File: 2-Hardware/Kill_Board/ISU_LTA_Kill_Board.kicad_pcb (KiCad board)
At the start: 2 copper layers, 157.5 x 36.2 mm, 30 parts, among them P1 CONN_01X02, P10 CONN_2, P11 CONN_2, P12 CONN_2, P2 CONN_01X02, P3 CONN_01X02, P4 CONN_01X03, P5 CONN_01X03, P6 CONN_01X03, P7 CONN_2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

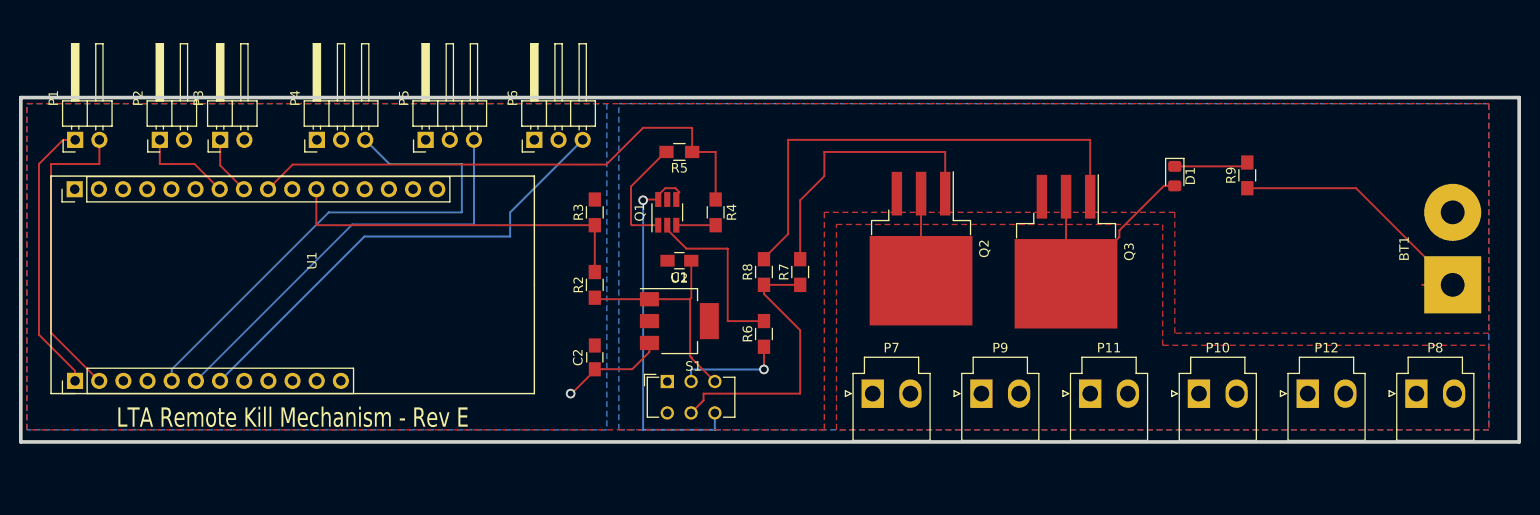
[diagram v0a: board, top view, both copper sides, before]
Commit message: Updated to have BEC and level shifter
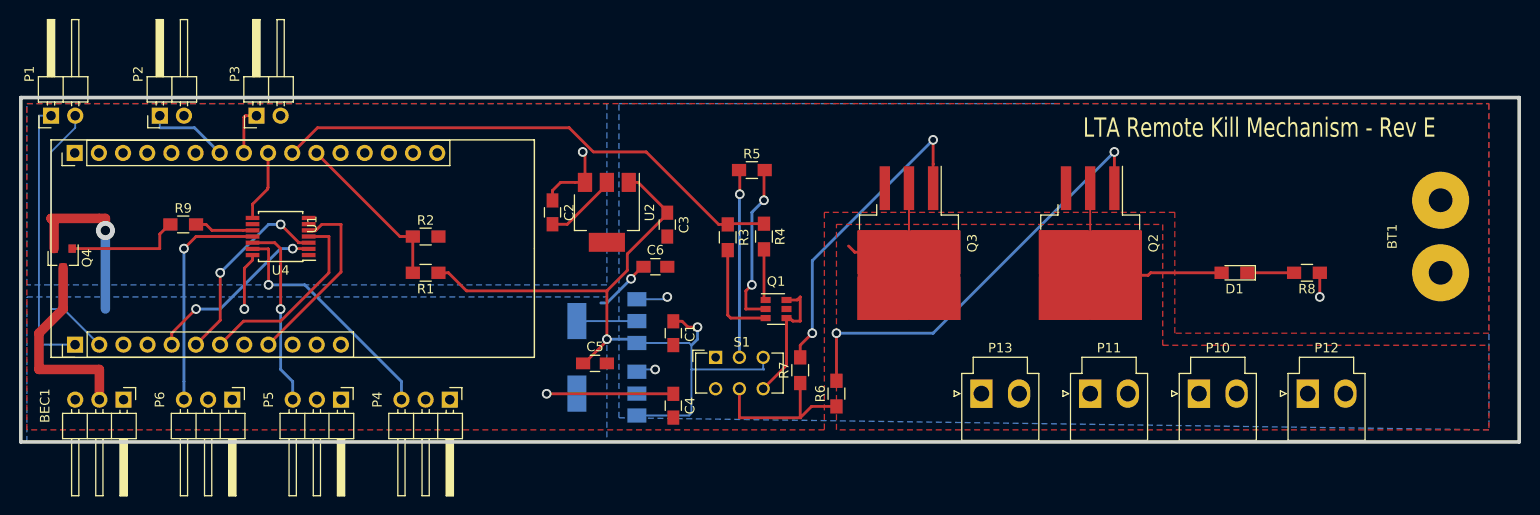
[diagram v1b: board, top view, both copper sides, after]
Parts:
- removed P7, P8, P9: CONN_2, Connectors_JST:JST_VH_B2P-VH-B_2x3.96mm_Vertical
- added BEC1: CONN_01X03, Pin_Headers:Pin_Header_Angled_1x03_Pitch2.54mm, F.Cu at (39.4, 95.9)
- added C3: 0.1uF, Capacitors_SMD:C_0805_HandSoldering, F.Cu at (96.5, 77.5)
- added C4: 10uF, Capacitors_SMD:C_0805_HandSoldering, F.Cu at (97.2, 96.5)
- added C5: 0.1uF, Capacitors_SMD:C_0805_HandSoldering, F.Cu at (88.9, 92.1)
- added C6: 10uF, Capacitors_SMD:C_0805_HandSoldering, F.Cu at (95.3, 81.9)
- added P13: CONN_2, Connectors_JST:JST_VH_B2P-VH-B_2x3.96mm_Vertical, F.Cu at (129.5, 95.2)
- added Q4: FDN359AN mfet, TO_SOT_Packages_SMD:SOT-23, F.Cu at (33.0, 81.0)
- added R1: 75K, Resistors_SMD:R_0805_HandSoldering, F.Cu at (71.1, 82.5)
- added U3: AZ1117-5.0, TO_SOT_Packages_SMD:SOT-223-3_TabPin2, B.Cu at (90.2, 95.2)
- added U4: NTS0104, Housings_SSOP:TSSOP-14_4.4x5mm_Pitch0.65mm, F.Cu at (55.9, 78.7)
- added U5: AZ1117-5.0, TO_SOT_Packages_SMD:SOT-223-3_TabPin2, B.Cu at (90.2, 87.6)
- BT1: footprint Connector_Wire:SolderWirePad_1x02_P7.62mm_Drill2.5mm -> Adafruit:SolderWirePad_2x_2-5mmDrill
- D1: footprint LED_SMD:LED_0805_2012Metric_Pad1.15x1.40mm_HandSolder -> LEDs:LED_0805_HandSoldering
- Q1: footprint Package_TO_SOT_SMD:SOT-23-6_Handsoldering -> TO_SOT_Packages_SMD:SOT-23-6
- Q2, Q3: footprint Package_TO_SOT_SMD:TO-263-3_TabPin2 -> TO_SOT_Packages_SMD:TO-263-3_TabPin2
- R2: value 75K -> 33k
- R3: value 33k -> 330
- R9: value 330 -> 2k
- S1: footprint Button_Switch_THT:SW_CuK_JS202011CQN_DPDT_Straight -> Buttons_Switches_ThroughHole:SW_CuK_JS202011CQN_DPDT_Straight
- U2: footprint Package_TO_SOT_SMD:SOT-223 -> TO_SOT_Packages_SMD:SOT-223
- moved R9 112.0 mm to (45.6, 77.5), turned to 0 degrees
- moved R8 57.1 mm to (163.8, 82.5), turned to 180 degrees
- moved P6 41.9 mm to (50.8, 95.9), turned to 270 degrees
- moved P4 30.7 mm to (73.7, 95.9), turned to 270 degrees
- moved P5 28.7 mm to (62.2, 95.9), turned to 270 degrees
- moved R2 18.5 mm to (71.1, 78.7), turned to 0 degrees
- moved Q2 17.8 mm to (141.0, 79.4)
- moved Q3 16.5 mm to (121.9, 79.4)
- moved C2 15.9 mm to (84.5, 76.2), turned to 270 degrees
- moved Q1 15.3 mm to (108.0, 86.4), turned to 0 degrees
- moved R3 14.2 mm to (102.9, 78.8), turned to 270 degrees
- moved U2 13.7 mm to (90.2, 76.2), turned to 270 degrees
- moved D1 11.9 mm to (156.1, 82.5), turned to 180 degrees
- moved R7 10.3 mm to (110.5, 92.8)
- moved R6 9.87 mm to (114.3, 95.2)
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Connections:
- P4 pad 2: +3.3V -> +5V
- P5 pad 2: +3.3V -> +5V
- P6 pad 2: +3.3V -> +5V
- R2 pad 1: Net-(C1-Pad1) -> /V_Sense
- R2 pad 2: /V_Sense -> GND
- R3 pad 1: /V_Sense -> /Ctrl
- R3 pad 2: GND -> Net-(Q1-Pad3)
- R4 pad 2: Net-(Q1-Pad3) -> Net-(Q1-Pad1)
- R5 pad 1: /Ctrl -> +BATT
- R5 pad 2: Net-(Q1-Pad1) -> Net-(Q1-Pad2)
- R6 pad 1: +BATT -> Net-(R6-Pad1)
- R6 pad 2: Net-(Q1-Pad2) -> Net-(Q2-Pad1)
- R7 pad 1: Net-(R7-Pad1) -> Net-(R6-Pad1)
- R7 pad 2: Net-(Q2-Pad1) -> Net-(Q3-Pad1)
- R8 pad 1: Net-(R7-Pad1) -> +BATT
- R8 pad 2: Net-(Q3-Pad1) -> Net-(D1-Pad1)
- R9 pad 1: +BATT -> Net-(Q4-Pad1)
- R9 pad 2: Net-(D1-Pad1) -> Net-(R9-Pad2)
- S1 pad 1: Net-(S1-Pad1) -> (no net)
- S1 pad 5: Net-(R7-Pad1) -> Net-(R6-Pad1)
- U1 pad 1: Net-(U1-Pad1) -> (no net)
- U1 pad 10: Net-(U1-Pad10) -> /Ctrl
- U1 pad 12: Net-(U1-Pad12) -> (no net)
- U1 pad 14: Net-(U1-Pad14) -> (no net)
- U1 pad 16: Net-(U1-Pad16) -> (no net)
- U1 pad 17: Net-(U1-Pad17) -> (no net)
- U1 pad 18: Net-(U1-Pad18) -> (no net)
- U1 pad 19: Net-(U1-Pad19) -> (no net)
- U1 pad 2: Net-(U1-Pad2) -> (no net)
- U1 pad 21: Net-(U1-Pad21) -> (no net)
- U1 pad 22: Net-(P6-Pad3) -> Net-(U1-Pad22)
- U1 pad 23: Net-(P5-Pad3) -> Net-(U1-Pad23)
- U1 pad 24: Net-(P4-Pad3) -> Net-(U1-Pad24)
- U1 pad 25: Net-(U1-Pad25) -> (no net)
- U1 pad 26: Net-(U1-Pad26) -> (no net)
- U1 pad 3: Net-(U1-Pad3) -> (no net)
- U1 pad 4: Net-(U1-Pad4) -> (no net)
- U1 pad 5: Net-(U1-Pad5) -> (no net)
- U1 pad 6: Net-(U1-Pad6) -> (no net)
- U1 pad 9: /Ctrl -> Net-(U1-Pad9)
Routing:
- net +5V: track 0.00 -> 56.6 mm, vias 0 -> 4
- net Net-(C1-Pad1): track 23.9 -> 79.5 mm, vias 0 -> 2
- net Net-(R7-Pad1): track 29.6 -> 0.00 mm
- net Net-(P4-Pad3): track 54.8 -> 25.5 mm, vias 0 -> 1
- net Net-(P6-Pad3): track 50.1 -> 23.6 mm, vias 0 -> 1
- net Net-(P5-Pad3): track 44.9 -> 19.6 mm, vias 0 -> 1
- net Net-(Q1-Pad4): track 39.2 -> 14.1 mm, vias 1 -> 0
- net Net-(BEC1-Pad2): track 0.00 -> 21.3 mm
- net Net-(U1-Pad23): track 0.00 -> 20.9 mm, vias 0 -> 2
- net Net-(U1-Pad22): track 0.00 -> 20.5 mm
- net /V_Sense: track 37.9 -> 17.6 mm
- net Net-(U1-Pad20): track 0.00 -> 19.5 mm
- net Net-(U1-Pad24): track 0.00 -> 19.3 mm, vias 0 -> 2
- net +BATT: track 40.3 -> 22.3 mm, vias 1 -> 2
- net Net-(Q3-Pad1): track 51.3 -> 33.7 mm, vias 0 -> 2
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- added copper zone on B.Cu, net +5V
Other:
- net class Default: clearance 0.0508 -> 0.01; trace_width 0.2032 -> 0.23
- rule pad_to_mask_clearance: 0.254 -> 0.4
- rule trace_clearance: 0.0508 -> 0.01

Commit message: FIxing pad clearence
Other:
- rule pad_to_mask_clearance: 0.4 -> 0.0508
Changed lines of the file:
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@@
     (mod_text_size 1.524 1.524)
     (mod_text_width 0.3048)
-    (pad_size 1.45 0.45)
-    (pad_drill 0)
-    (pad_to_mask_clearance 0.4)
+    (pad_size 1.45 1.45)
+    (pad_drill 0.5)
+    (pad_to_mask_clearance 0.0508)
     (solder_mask_min_width 0.25)
     (aux_axis_origin 0 0)
@@
     (model ${KISYS3DMOD}/TO_SOT_Packages_SMD.3dshapes/SOT-223.wrl
       (at (xyz 0 0 0))
-      (scale (xyz 1 1 1))
-      (rotate (xyz 0 0 0))
+      (scale (xyz 0.4 0.4 0.4))
+      (rotate (xyz 0 0 90))
     )
   )
@@
     (model ${KISYS3DMOD}/TO_SOT_Packages_SMD.3dshapes/SOT-223.wrl
       (at (xyz 0 0 0))
-      (scale (xyz 1 1 1))
-      (rotate (xyz 0 0 0))
+      (scale (xyz 0.4 0.4 0.4))
+      (rotate (xyz 0 0 90))
     )
   )
@@
     (model ${KISYS3DMOD}/TO_SOT_Packages_SMD.3dshapes/SOT-223.wrl
       (at (xyz 0 0 0))
-      (scale (xyz 1 1 1))
-      (rotate (xyz 0 0 0))
-    )
-  )
+      (scale (xyz 0.4 0.4 0.4))
+      (rotate (xyz 0 0 90))
+    )
+  )
